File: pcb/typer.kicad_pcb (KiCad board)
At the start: 2 copper layers, 182.8 x 158.9 mm, 48 parts, among them J2 3.5mm, SW0:10 SW0:3, SW0:11 SW0:2, SW0:12 SW0:1, SW0:7 SW0:6, SW0:8 SW0:5, SW0:9 SW0:4, SW1:10 SW1:3, SW1:11 SW1:2, SW1:12 SW1:1, SW1:13 SW1:0, SW1:9 SW1:4, SW2:10 SW2:3, SW2:11 SW2:2, SW2:12 SW2:1, SW2:13 SW2:0, SW2:7 SW2:6, SW2:8 SW2:5, SW2:9 SW2:4, SW3:10 SW3:3, SW3:11 SW3:2, SW3:12 SW3:1, SW3:13 SW3:0, SW3:8 SW3:5, SW3:9 SW3:4, SW4:10 SW4:3, SW4:11 SW4:2, SW4:12 SW4:1, SW4:13 SW4:0, SW4:7 SW4:6, SW4:8 SW4:5, SW4:9 SW4:4, SW5:10 SW5:3, SW5:11 SW5:2, SW5:12 SW5:1, SW5:13 SW5:0, SW5:7 SW5:6, SW5:8 SW5:5, SW5:9 SW5:4

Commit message: lib change
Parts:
- D1:7, D1:8: footprint DIODE -> Library:DIODE
- H99: footprint ErgoDOXmech -> Library:ErgoDOXmech
- J2: footprint 4pin35mmAudio -> Library:4pin35mmAudio
- S1, S2: footprint STAB_PCB940 -> Library:STAB_PCB940
- SW0:10, SW0:11, SW0:12, SW0:7, SW0:8, SW0:9, SW1:10, SW1:11, SW1:12, SW1:13, SW1:9, SW2:10, SW2:11, SW2:12, SW2:7, SW2:8, SW2:9, SW3:10, SW3:11, SW3:12, SW3:8, SW3:9, SW4:10, SW4:11, SW4:12, SW4:7, SW4:8, SW4:9, SW5:10, SW5:11, SW5:12, SW5:7, SW5:8, SW5:9: footprint ErgoDOX pcb:MX_FLIP_DIODE -> Library:MX_FLIP_DIODE
- SW2:13, SW3:13, SW4:13, SW5:13: footprint ErgoDOX pcb:MX_FLIP_XX -> Library:MX_FLIP_XX
- SX0:10, SX0:11, SX1:7, SX1:8: footprint MX_FLIP -> Library:MX_FLIP

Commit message: new project updates
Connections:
- J2 pad 1: Net-(J1-Pad5) -> unconnected-(J2-Pad1)
- J2 pad 2: /SDAM -> unconnected-(J2-Pad2)
- J2 pad 3: /SCLM -> unconnected-(J2-Pad3)
- J2 pad 4: Net-(J1-Pad1) -> unconnected-(J2-Pad4)
- J2 pad 5: /SCLM -> unconnected-(J2-Pad5)
- J2 pad 6: /SDAM -> unconnected-(J2-Pad6)
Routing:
- net (no net): track 682.7 -> 934.0 mm
- net /SDAM: track 128.3 -> 0.00 mm
- net /SCLM: track 119.7 -> 0.00 mm
- net Net-(J1-Pad1): track 102.6 -> 0.00 mm
- net unconnected-(J2-Pad4): track 0.00 -> 99.2 mm
- net unconnected-(J2-Pad1): track 0.00 -> 62.3 mm
- net Net-(J1-Pad5): track 62.3 -> 0.00 mm

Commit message: placement update
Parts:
- removed D1:7, D1:8: D, Library:DIODE
- removed SW0:10: SW0:3, Library:MX_FLIP_DIODE
- removed SW0:11: SW0:2, Library:MX_FLIP_DIODE
- removed SW0:12: SW0:1, Library:MX_FLIP_DIODE
- removed SW0:7: SW0:6, Library:MX_FLIP_DIODE
- removed SW0:8: SW0:5, Library:MX_FLIP_DIODE
- removed SW0:9: SW0:4, Library:MX_FLIP_DIODE
- removed SW1:10: SW1:3, Library:MX_FLIP_DIODE
- removed SW1:11: SW1:2, Library:MX_FLIP_DIODE
- removed SW1:12: SW1:1, Library:MX_FLIP_DIODE
- removed SW1:13: SW1:0, Library:MX_FLIP_DIODE
- removed SW1:9: SW1:4, Library:MX_FLIP_DIODE
- removed SW2:10: SW2:3, Library:MX_FLIP_DIODE
- removed SW2:11: SW2:2, Library:MX_FLIP_DIODE
- removed SW2:12: SW2:1, Library:MX_FLIP_DIODE
- removed SW2:13: SW2:0, Library:MX_FLIP_XX
- removed SW2:7: SW2:6, Library:MX_FLIP_DIODE
- removed SW2:8: SW2:5, Library:MX_FLIP_DIODE
- removed SW2:9: SW2:4, Library:MX_FLIP_DIODE
- removed SW3:10: SW3:3, Library:MX_FLIP_DIODE
- removed SW3:11: SW3:2, Library:MX_FLIP_DIODE
- removed SW3:12: SW3:1, Library:MX_FLIP_DIODE
- removed SW3:13: SW3:0, Library:MX_FLIP_XX
- removed SW3:8: SW3:5, Library:MX_FLIP_DIODE
- removed SW3:9: SW3:4, Library:MX_FLIP_DIODE
- removed SW4:10: SW4:3, Library:MX_FLIP_DIODE
- removed SW4:11: SW4:2, Library:MX_FLIP_DIODE
- removed SW4:12: SW4:1, Library:MX_FLIP_DIODE
- removed SW4:13: SW4:0, Library:MX_FLIP_XX
- removed SW4:7: SW4:6, Library:MX_FLIP_DIODE
- removed SW4:8: SW4:5, Library:MX_FLIP_DIODE
- removed SW4:9: SW4:4, Library:MX_FLIP_DIODE
- removed SW5:10: SW5:3, Library:MX_FLIP_DIODE
- removed SW5:11: SW5:2, Library:MX_FLIP_DIODE
- removed SW5:12: SW5:1, Library:MX_FLIP_DIODE
- removed SW5:13: SW5:0, Library:MX_FLIP_XX
- removed SW5:7: SW5:6, Library:MX_FLIP_DIODE
- removed SW5:8: SW5:5, Library:MX_FLIP_DIODE
- removed SW5:9: SW5:4, Library:MX_FLIP_DIODE
- removed SX0:10: SX0:3, Library:MX_FLIP
- removed SX0:11: SX0:2, Library:MX_FLIP
- removed SX1:7: SX1:6, Library:MX_FLIP
- removed SX1:8: SX1:5, Library:MX_FLIP
- added SW0:0: SW0:0, Library:MX_FLIP_XX, F.Cu at (191.5, 67.0)
- added SW0:1: SW0:1, Library:MX_FLIP_XX, F.Cu at (191.5, 86.1)
- added SW0:2: SW0:2, Library:MX_FLIP_XX, F.Cu at (191.5, 105.1)
- added SW0:3: SW0:3, Library:MX_FLIP_XX, F.Cu at (191.5, 124.2)
- added SW0:4: SW0:4, Library:MX_FLIP_DIODE, F.Cu at (186.7, 143.2)
- added SW1:0: SW1:0, Library:MX_FLIP_DIODE, F.Cu at (167.6, 67.0)
- added SW1:1: SW1:1, Library:MX_FLIP_DIODE, F.Cu at (167.6, 86.1)
- added SW1:2: SW1:2, Library:MX_FLIP_DIODE, F.Cu at (167.6, 105.1)
- added SW1:3: SW1:3, Library:MX_FLIP_DIODE, F.Cu at (167.6, 124.2)
- added SW1:4: SW1:4, Library:MX_FLIP_DIODE, F.Cu at (167.6, 143.2)
- added SW2:0: SW2:0, Library:MX_FLIP_DIODE, F.Cu at (148.6, 63.8)
- added SW2:1: SW2:1, Library:MX_FLIP_DIODE, F.Cu at (148.6, 82.9)
- added SW2:2: SW2:2, Library:MX_FLIP_DIODE, F.Cu at (148.6, 101.9)
- added SW2:3: SW2:3, Library:MX_FLIP_DIODE, F.Cu at (148.6, 121.0)
- added SW2:4: SW2:4, Library:MX_FLIP_DIODE, F.Cu at (148.6, 140.0)
- added SW3:0: SW3:0, Library:MX_FLIP_DIODE, F.Cu at (129.5, 62.2)
- added SW3:1: SW3:1, Library:MX_FLIP_DIODE, F.Cu at (129.5, 81.3)
- added SW3:2: SW3:2, Library:MX_FLIP_DIODE, F.Cu at (129.5, 100.3)
- added SW3:3: SW3:3, Library:MX_FLIP_DIODE, F.Cu at (129.5, 119.4)
- added SW3:4: SW3:4, Library:MX_FLIP_DIODE, F.Cu at (129.5, 138.4)
- added SW4:0: SW4:0, Library:MX_FLIP_DIODE, F.Cu at (110.5, 63.8)
- added SW4:1: SW4:1, Library:MX_FLIP_DIODE, F.Cu at (110.5, 82.9)
- added SW4:2: SW4:2, Library:MX_FLIP_DIODE, F.Cu at (110.5, 101.9)
- added SW4:3: SW4:3, Library:MX_FLIP_DIODE, F.Cu at (110.5, 121.0)
- added SW4:4: SW4:4, Library:MX_FLIP_DIODE, F.Cu at (110.5, 140.0)
- added SW5:0: SW5:0, Library:MX_FLIP_DIODE, F.Cu at (91.4, 65.1)
- added SW5:1: SW5:1, Library:MX_FLIP_DIODE, F.Cu at (91.4, 84.1)
- added SW5:2: SW5:2, Library:MX_FLIP_DIODE, F.Cu at (91.4, 103.2)
- added SW5:3: SW5:3, Library:MX_FLIP_DIODE, F.Cu at (91.4, 122.2)
- added SW5:4: SW5:4, Library:MX_FLIP_DIODE, F.Cu at (81.3, 153.1)
- added SW6:0: SW6:0, Library:MX_FLIP_DIODE, F.Cu at (72.4, 65.1)
- added SW6:1: SW6:1, Library:MX_FLIP_DIODE, F.Cu at (72.4, 88.9)
- added SW6:2: SW6:2, Library:MX_FLIP_DIODE, F.Cu at (72.4, 117.5)
- added SW6:3: SW6:3, Library:MX_FLIP_DIODE, F.Cu at (52.0, 135.2)
- added SW6:4: SW6:4, Library:MX_FLIP_DIODE, F.Cu at (64.0, 161.1)
- added SW7:2: SW7:2, Library:MX_FLIP_DIODE, F.Cu at (34.7, 143.3)
- added SW7:3: SW7:3, Library:MX_FLIP_DIODE, F.Cu at (42.7, 160.5)
- added SW7:4: SW7:4, Library:MX_FLIP_DIODE, F.Cu at (50.8, 177.8)
- added SX5:4: SX5:4, Library:MX_FLIP, F.Cu at (77.3, 144.4)
- added SX6:4: SX6:4, Library:MX_FLIP, F.Cu at (60.0, 152.5)
- added SY5:4: SY5:4, Library:MX_FLIP, F.Cu at (85.3, 161.7)
- added SY6:4: SY6:4, Library:MX_FLIP, F.Cu at (68.1, 169.7)
- moved J2 0.21 mm to (86.4, 30.6)
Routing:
- net (no net): track 934.0 -> 0.00 mm, vias 2 -> 0
- net /ROW0: track 404.2 -> 0.00 mm
- net /ROW1: track 318.2 -> 0.00 mm
- net /COL11: track 316.5 -> 0.00 mm
- net /ROW2: track 295.3 -> 0.00 mm
- net /COL1: track 291.8 -> 0.00 mm
- net /COL4: track 274.3 -> 0.00 mm
- net /COL6: track 259.5 -> 0.00 mm
- net /ROW4: track 257.4 -> 0.00 mm
- net /ROW3: track 238.7 -> 0.00 mm
- net /COL10: track 233.7 -> 0.00 mm
- net /COL5: track 225.8 -> 0.00 mm
- net /ROW5: track 225.1 -> 0.00 mm
- net /COL0: track 159.7 -> 0.00 mm
- net COLUMN0: track 0.00 -> 112.6 mm
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
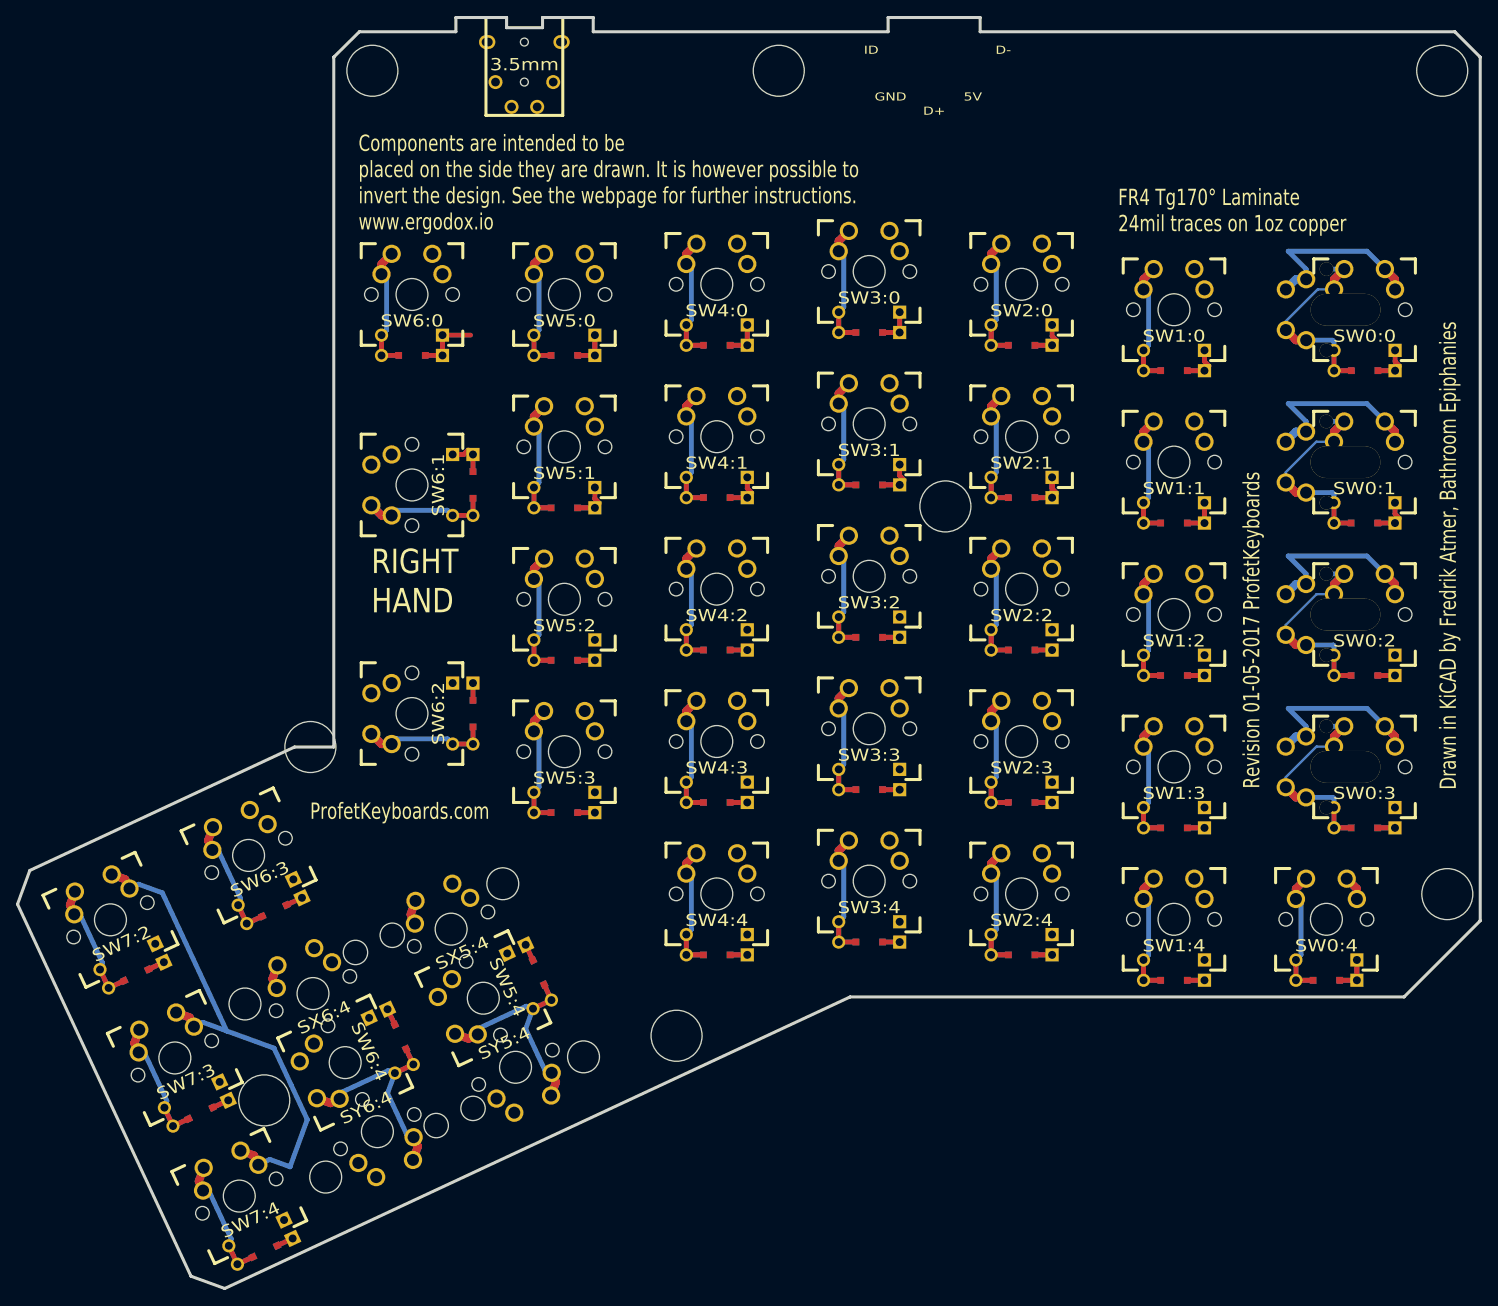
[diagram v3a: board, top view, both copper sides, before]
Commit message: start track layout
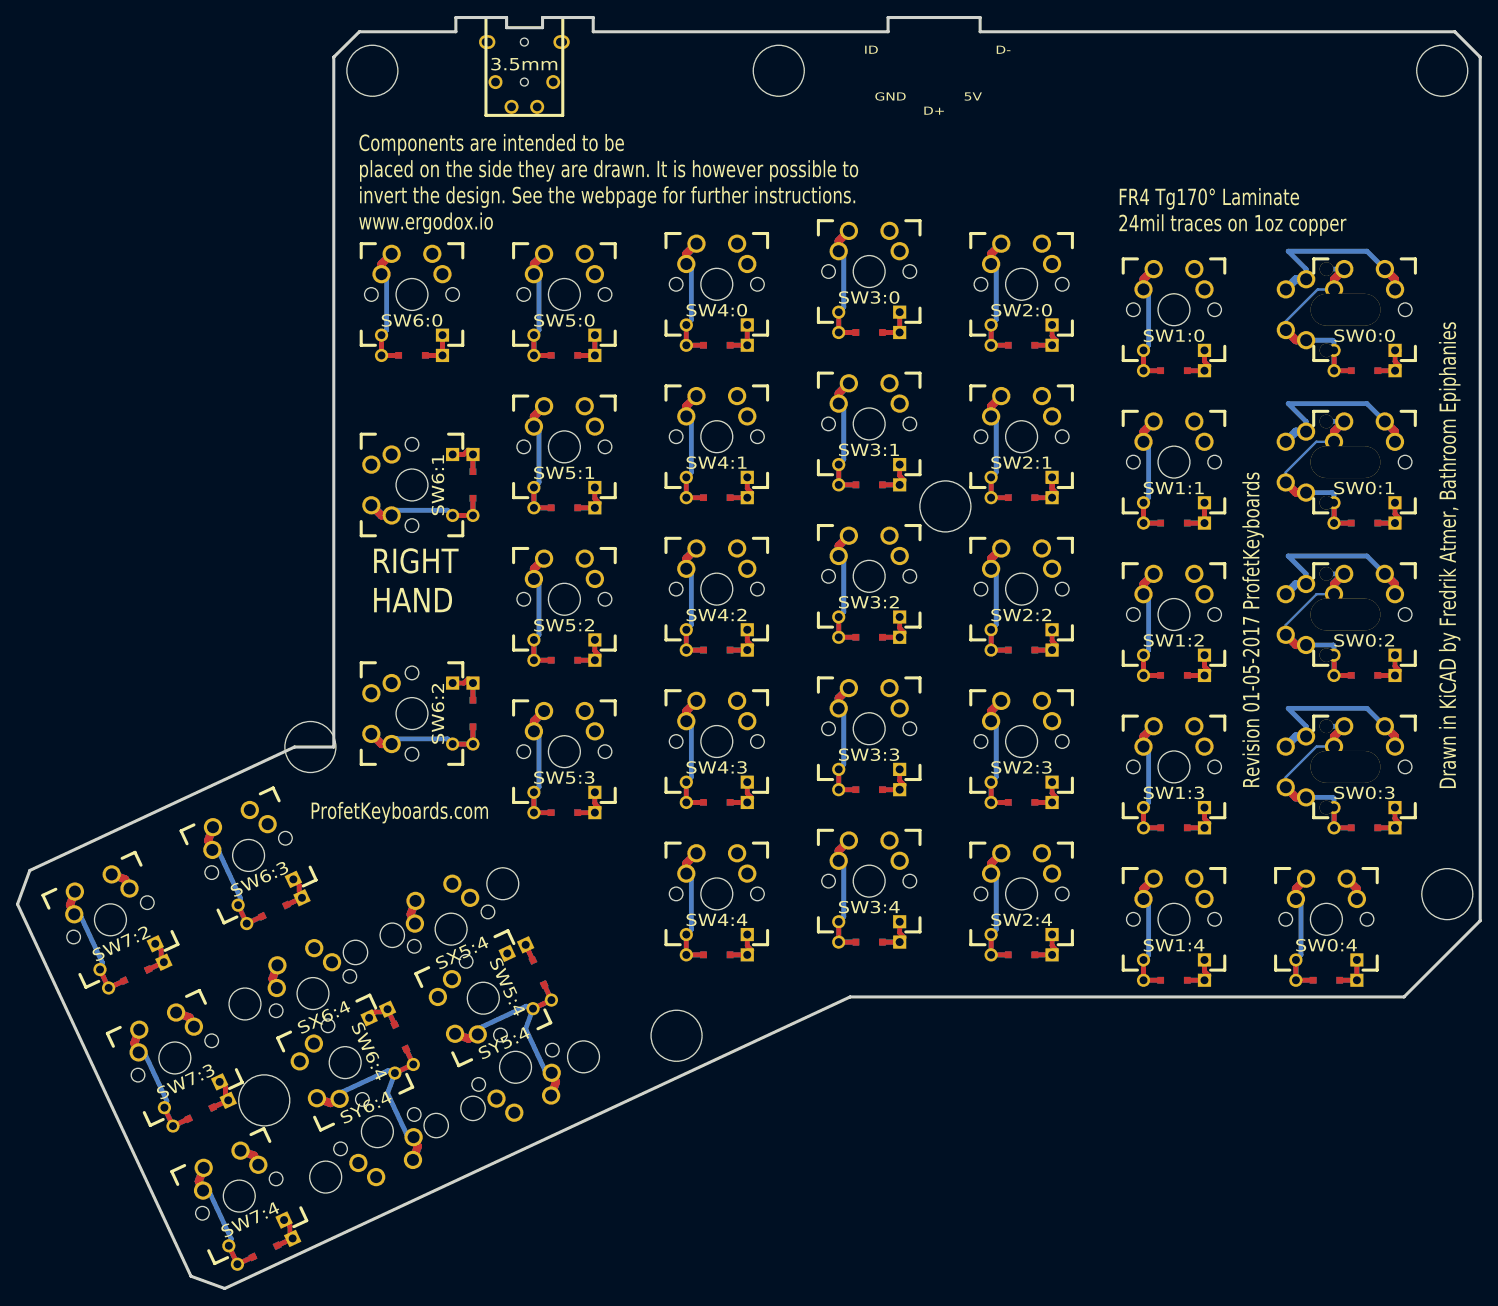
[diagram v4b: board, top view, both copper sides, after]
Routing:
- net COLUMN7: track 73.0 -> 18.4 mm
- net ROW2: track 0.00 -> 17.3 mm
- net ROW4: track 5.08 -> 17.6 mm
- net ROW0: track 30.4 -> 27.5 mm
- net unconnected-(SW3:3-K-Pad4): track 0.00 -> 2.20 mm
- net unconnected-(SW4:3-K-Pad4): track 0.00 -> 2.20 mm
- net unconnected-(SW2:3-K-Pad4): track 0.00 -> 2.20 mm
- net unconnected-(SW5:3-K-Pad4): track 0.00 -> 2.20 mm
- net unconnected-(SW1:3-K-Pad4): track 0.00 -> 2.20 mm
- net unconnected-(SW0:3-K-Pad4): track 0.00 -> 2.20 mm
- net unconnected-(SW6:3-K-Pad4): track 0.00 -> 1.87 mm
- net ROW3: track 0.00 -> 1.87 mm

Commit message: row track layout added
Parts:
- added U1: rp2040-zero, mcu:rp2040-zero-tht, F.Cu at (137.3, 44.0)
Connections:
- SW0:3 pad 4: unconnected-(SW0:3-K-Pad4) -> ROW3
- SW1:3 pad 4: unconnected-(SW1:3-K-Pad4) -> ROW3
- SW2:3 pad 4: unconnected-(SW2:3-K-Pad4) -> ROW3
- SW3:3 pad 4: unconnected-(SW3:3-K-Pad4) -> ROW3
- SW4:3 pad 4: unconnected-(SW4:3-K-Pad4) -> ROW3
- SW5:3 pad 4: unconnected-(SW5:3-K-Pad4) -> ROW3
- SW6:3 pad 4: unconnected-(SW6:3-K-Pad4) -> ROW3
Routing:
- net ROW3: track 1.87 -> 235.9 mm
- net ROW2: track 17.3 -> 234.2 mm
- net ROW4: track 17.6 -> 188.8 mm
- net ROW1: track 23.4 -> 193.5 mm
- net ROW0: track 27.5 -> 195.3 mm
- net unconnected-(SW3:3-K-Pad4): track 2.20 -> 0.00 mm
- net unconnected-(SW4:3-K-Pad4): track 2.20 -> 0.00 mm
- net unconnected-(SW2:3-K-Pad4): track 2.20 -> 0.00 mm
- net unconnected-(SW5:3-K-Pad4): track 2.20 -> 0.00 mm
- net unconnected-(SW1:3-K-Pad4): track 2.20 -> 0.00 mm
- net unconnected-(SW0:3-K-Pad4): track 2.20 -> 0.00 mm
- net unconnected-(SW6:3-K-Pad4): track 1.87 -> 0.00 mm
